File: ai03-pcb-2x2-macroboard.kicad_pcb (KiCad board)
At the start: 2 copper layers, 24 parts, among them SW1 SW_Push, U1 ATmega32U4-AU, Y1 16MHz

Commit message: Place Components
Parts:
- F1: value Polyfuse -> 500Am; moved to B.Cu
- R1: value R_Small -> 10k; moved to B.Cu
- R2, R3, SW1, USB1: moved to B.Cu
- moved SW1 60.7 mm to (107.2, 99.2)
- moved R1 51.4 mm to (110.3, 82.5), turned to 90 degrees
- moved R3 45.6 mm to (101.6, 82.5), turned to 90 degrees
- moved USB1 45.1 mm to (103.9, 73.3), turned to 270 degrees
- moved F1 44.7 mm to (96.0, 82.5), turned to 270 degrees
- moved R2 40.4 mm to (105.6, 82.5), turned to 90 degrees
- moved R4 32.6 mm to (131.8, 93.7)
- moved C3 9.56 mm to (111.1, 89.7)
- moved C5 9.56 mm to (132.6, 85.7)
- moved C1 9.56 mm to (126.2, 77.0)
- moved C2 9.56 mm to (118.3, 77.0)
- moved C4 9.56 mm to (113.5, 82.5)
- moved C6 9.56 mm to (127.1, 100.8)
- moved C7 9.56 mm to (117.5, 100.8)
- moved U1 9.56 mm to (122.4, 90.1)
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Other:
- board outline added: 80.2 x 38.1 mm

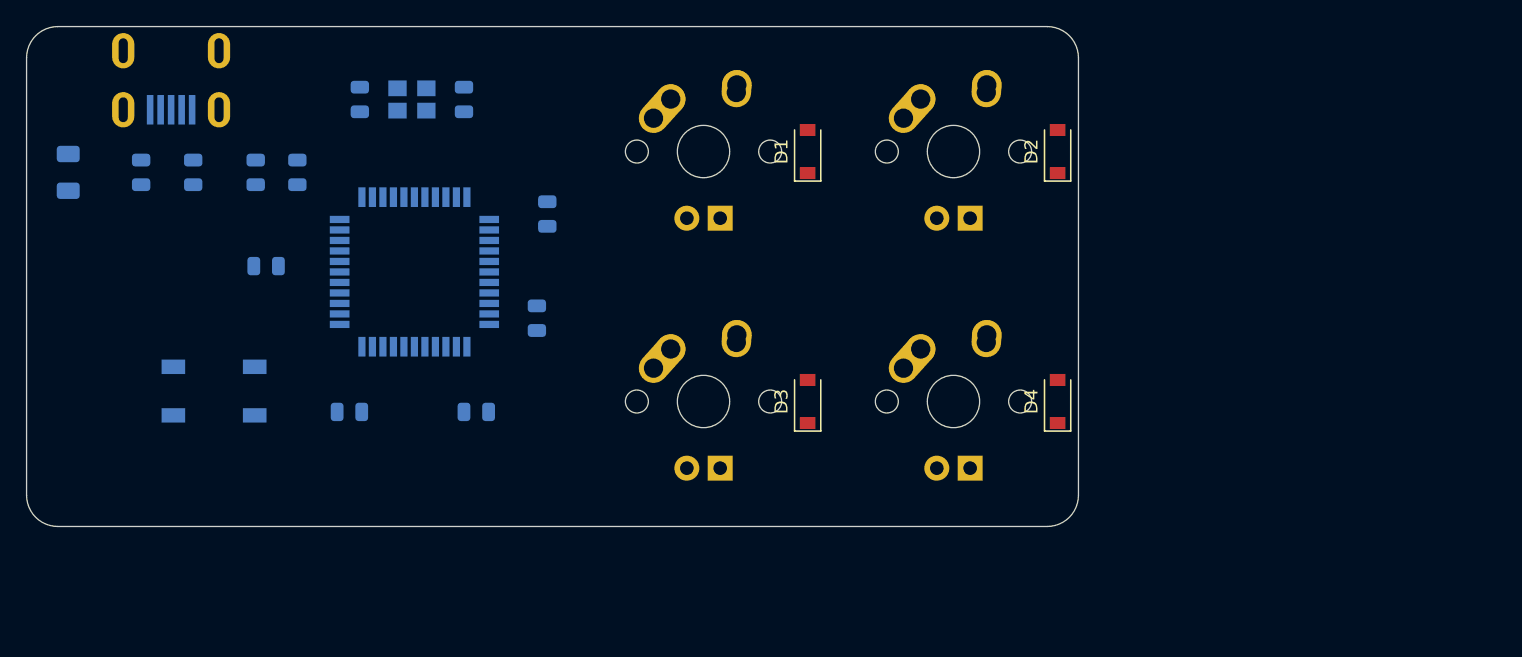
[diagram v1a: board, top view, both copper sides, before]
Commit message: Re-Place Components
Placement was too bad -> Do it again!
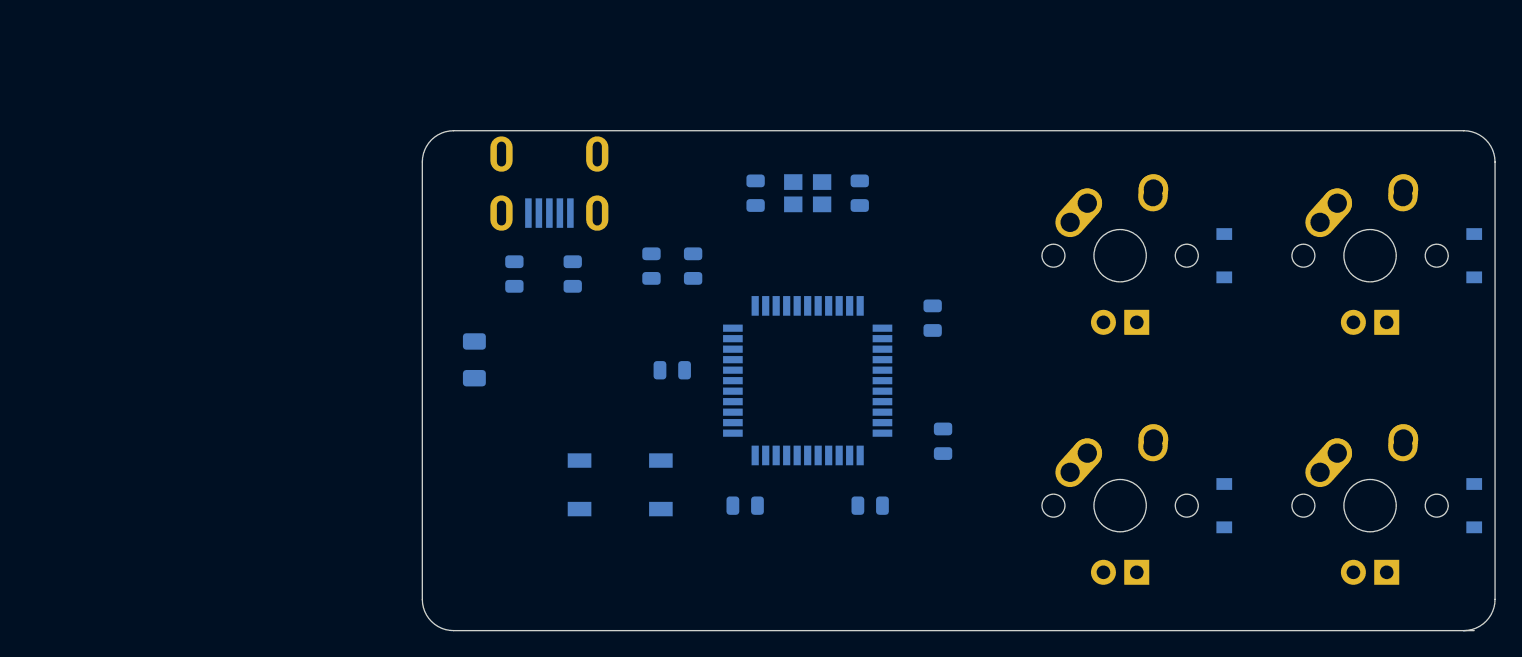
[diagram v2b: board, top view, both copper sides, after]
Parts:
- D1, D2, D3, D4: moved to B.Cu
- F1: value 500Am -> 500mA
- moved F1 34.1 mm to (127.0, 96.8)
- moved D1 32.7 mm to (184.2, 88.9)
- moved D2 32.7 mm to (203.2, 88.9)
- moved D3 32.7 mm to (184.2, 108.0)
- moved D4 32.7 mm to (203.2, 108.0)
- moved MX1 32.7 mm to (176.2, 88.9)
- moved MX2 32.7 mm to (195.3, 88.9)
- moved MX3 32.7 mm to (176.2, 108.0)
- moved MX4 32.7 mm to (195.3, 108.0)
- moved R4 32.3 mm to (162.7, 103.0)
- moved C3 32.0 mm to (142.1, 97.6), turned to 0 degrees
- moved SW1 31.8 mm to (138.1, 106.4), turned to 180 degrees
- moved U1 31.1 mm to (152.4, 98.4)
- moved C1 31.0 mm to (156.4, 84.1), turned to 270 degrees
- moved C2 31.0 mm to (148.4, 84.1), turned to 90 degrees
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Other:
- board size 80.2 x 38.1 mm -> 81.8 x 38.1 mm

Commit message: Add Routing
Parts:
- moved C7 7.49 mm to (141.3, 104.0), turned to 270 degrees
- moved SW1 7.10 mm to (131.8, 109.5)
- moved R2 0.92 mm to (133.7, 90.8)
- moved R3 0.62 mm to (130.4, 90.8)
- moved USB1 0.28 mm to (132.5, 81.0)
- turned F1 to 90 degrees
- turned R1 to 270 degrees
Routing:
- net GND: track 0.00 -> 152.4 mm
- net +5V: track 0.00 -> 108.2 mm, vias 0 -> 5
- net ROW1: track 0.00 -> 55.5 mm
- net COL1: track 0.00 -> 55.4 mm
- net ROW0: track 0.00 -> 50.4 mm
- net COL0: track 0.00 -> 36.2 mm
- net Net-(R1-Pad2): track 0.00 -> 32.0 mm, vias 0 -> 2
- net Net-(R3-Pad1): track 0.00 -> 22.3 mm
- net Net-(R2-Pad1): track 0.00 -> 21.5 mm
- net Net-(C2-Pad2): track 0.00 -> 14.2 mm
- net VCC: track 0.00 -> 11.5 mm
- net Net-(C1-Pad2): track 0.00 -> 11.2 mm
- net Net-(D2-Pad2): track 0.00 -> 7.51 mm
- net Net-(D4-Pad2): track 0.00 -> 7.51 mm
- net Net-(D1-Pad2): track 0.00 -> 6.82 mm
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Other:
- net class Default: trace_width 0.25 -> 0.254
- net class Power added: clearance 0.2, trace_width 0.381, via_dia 0.8, via_drill 0.4

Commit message: Add Gerber-Files
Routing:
- net +5V: track 108.2 -> 113.1 mm
- net GND: track 152.4 -> 150.3 mm
- net ROW1: track 55.5 -> 54.0 mm
- net ROW0: track 50.4 -> 48.9 mm
- net Net-(D3-Pad2): track 6.82 -> 7.94 mm
- net Net-(D1-Pad2): track 6.82 -> 7.64 mm
- net Net-(D4-Pad2): track 7.51 -> 8.07 mm
- added copper zone on B.Cu, net GND
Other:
- outline, holes or cut-outs redrawn
- board text added: "Hello, PCB-World!"
- board text added: "MX1"
- board text added: "MX2"
- board text added: "MX3"
- board text added: "MX4"
